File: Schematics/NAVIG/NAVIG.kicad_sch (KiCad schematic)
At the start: 73 parts, among them J1 SWD, J12 GNSS_SMA, J13 3.3V IN, J13 USART, J14 CNTRL I2C, J6 USB_C_Receptacle_USB2.0, SW2 Omron_B3F-10xx, U11 BMP390, U4 BNO055, U4 STM32F205RETx, U7 NEO-M9N, U8 USBLC6-2SC6, Y1 12MHz_ECS-120-18-33-JGN-TR3, Y2 32.768KHz

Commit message: slight fixes to navig board for final production run
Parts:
- added J7: Reset Jumper, Connector_PinHeader_2.54mm:PinHeader_1x02_P2.54mm_Vertical, symbol Connector_Generic:Conn_01x02
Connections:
- net SWD_NRST: now also J7.1 (Pin_1); no longer SW2.1
- new net: J7.2 (Pin_2), SW2.1
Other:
- moved on the sheet: R1, SW2
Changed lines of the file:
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@@
   (junction (at 144.78 38.1) (diameter 0) (color 0 0 0 0)
   )
-  (junction (at 43.18 64.77) (diameter 0) (color 0 0 0 0)
+  (junction (at 43.18 60.96) (diameter 0) (color 0 0 0 0)
   )
   (junction (at 53.34 149.86) (diameter 0) (color 0 0 0 0)
@@
     (stroke (width 0) (type default))
   )
-  (wire (pts (xy 43.18 64.77) (xy 39.37 64.77))
+  (wire (pts (xy 43.18 60.96) (xy 39.37 60.96))
     (stroke (width 0) (type default))
   )
@@
     (stroke (width 0) (type default))
   )
+  (wire (pts (xy 44.45 81.28) (xy 55.88 81.28))
+    (stroke (width 0) (type default))
+  )
   (wire (pts (xy 133.35 38.1) (xy 133.35 36.83))
     (stroke (width 0) (type default))
@@
     (stroke (width 0) (type default))
   )
-  (wire (pts (xy 54.61 64.77) (xy 58.42 64.77))
+  (wire (pts (xy 54.61 60.96) (xy 58.42 60.96))
     (stroke (width 0) (type default))
   )
@@
     (stroke (width 0) (type default))
   )
-  (wire (pts (xy 39.37 81.28) (xy 55.88 81.28))
+  (wire (pts (xy 39.37 81.28) (xy 41.91 81.28))
     (stroke (width 0) (type default))
   )
@@
     (stroke (width 0) (type default))
   )
-  (wire (pts (xy 46.99 64.77) (xy 43.18 64.77))
+  (wire (pts (xy 46.99 60.96) (xy 43.18 60.96))
     (stroke (width 0) (type default))
   )
@@
     (stroke (width 0) (type default))
   )
-  (wire (pts (xy 43.18 58.42) (xy 43.18 64.77))
+  (wire (pts (xy 43.18 54.61) (xy 43.18 60.96))
     (stroke (width 0) (type default))
   )
@@
     (stroke (width 0) (type default))
   )
-  (rectangle (start 25.4 49.53) (end 71.12 73.66)
+  (rectangle (start 25.4 45.72) (end 71.12 69.85)
     (stroke (width 0) (type default))
     (fill (type none))
@@
     (fill (type none))
   )
-  (rectangle (start 25.4 76.2) (end 71.12 95.25)
+  (rectangle (start 25.4 72.39) (end 71.12 95.25)
     (stroke (width 0) (type default))
     (fill (type none))
@@
     (effects (font (size 3 3) bold) (justify left bottom))
   )
-  (text "BOOT0" (at 26.67 53.34 0)
+  (text "BOOT0" (at 26.67 49.53 0)
     (effects (font (size 2 2)) (justify left bottom))
   )
-  (text "MCU RESET" (at 53.34 80.01 0)
+  (text "MCU RESET" (at 53.34 76.2 0)
     (effects (font (size 2 2)) (justify left bottom))
   )
@@
     )
   )
-  (global_label "BOOT0" (shape input) (at 39.37 64.77 180) (fields_autoplaced)
+  (global_label "BOOT0" (shape input) (at 39.37 60.96 180) (fields_autoplaced)
     (effects (font (size 1.27 1.27)) (justify right))
-    (property "Intersheetrefs" "${INTERSHEET_REFS}" (at 30.2767 64.77 0)
+    (property "Intersheetrefs" "${INTERSHEET_REFS}" (at 30.2767 60.96 0)
       (effects (font (size 1.27 1.27)) (justify right) hide)
     )
@@
     )
   )
-  (symbol (lib_id "power:+3.3V") (at 53.34 58.42 270) (unit 1)
+  (symbol (lib_id "power:+3.3V") (at 53.34 54.61 270) (unit 1)
     (in_bom yes) (on_board yes) (dnp no) (fields_autoplaced)
-    (property "Reference" "#PWR07" (at 49.53 58.42 0)
+    (property "Reference" "#PWR07" (at 49.53 54.61 0)
       (effects (font (size 1.27 1.27)) hide)
     )
-    (property "Value" "+3.3V" (at 57.15 58.42 90)
+    (property "Value" "+3.3V" (at 57.15 54.61 90)
       (effects (font (size 1.27 1.27)) (justify left))
     )
-    (property "Footprint" "" (at 53.34 58.42 0)
+    (property "Footprint" "" (at 53.34 54.61 0)
       (effects (font (size 1.27 1.27)) hide)
     )
-    (property "Datasheet" "" (at 53.34 58.42 0)
+    (property "Datasheet" "" (at 53.34 54.61 0)
       (effects (font (size 1.27 1.27)) hide)
     )
@@
     )
   )
-  (symbol (lib_id "power:GND") (at 58.42 64.77 90) (unit 1)
+  (symbol (lib_id "power:GND") (at 58.42 60.96 90) (unit 1)
     (in_bom yes) (on_board yes) (dnp no) (fields_autoplaced)
-    (property "Reference" "#PWR06" (at 64.77 64.77 0)
+    (property "Reference" "#PWR06" (at 64.77 60.96 0)
       (effects (font (size 1.27 1.27)) hide)
     )
-    (property "Value" "GND" (at 62.23 64.77 90)
+    (property "Value" "GND" (at 62.23 60.96 90)
       (effects (font (size 1.27 1.27)) (justify right))
     )
-    (property "Footprint" "" (at 58.42 64.77 0)
+    (property "Footprint" "" (at 58.42 60.96 0)
       (effects (font (size 1.27 1.27)) hide)
     )
-    (property "Datasheet" "" (at 58.42 64.77 0)
+    (property "Datasheet" "" (at 58.42 60.96 0)
       (effects (font (size 1.27 1.27)) hide)
     )
@@
     )
   )
-  (symbol (lib_id "Device:R") (at 50.8 64.77 90) (unit 1)
+  (symbol (lib_id "Device:R") (at 50.8 60.96 90) (unit 1)
     (in_bom yes) (on_board yes) (dnp no)
-    (property "Reference" "R1" (at 50.8 67.31 90)
+    (property "Reference" "R1" (at 50.8 63.5 90)
       (effects (font (size 1.27 1.27)))
     )
-    (property "Value" "100K" (at 50.8 62.23 90)
+    (property "Value" "100K" (at 50.8 58.42 90)
       (effects (font (size 1.27 1.27)))
     )
-    (property "Footprint" "Resistor_SMD:R_0603_1608Metric" (at 50.8 66.548 90)
+    (property "Footprint" "Resistor_SMD:R_0603_1608Metric" (at 50.8 62.738 90)
       (effects (font (size 1.27 1.27)) hide)
     )
-    (property "Datasheet" "~" (at 50.8 64.77 0)
+    (property "Datasheet" "~" (at 50.8 60.96 0)
       (effects (font (size 1.27 1.27)) hide)
     )
@@
     )
   )
+  (symbol (lib_id "Connector_Generic:Conn_01x02") (at 41.91 76.2 90) (unit 1)
+    (in_bom yes) (on_board yes) (dnp no) (fields_autoplaced)
+    (property "Reference" "J7" (at 46.99 74.93 90)
+      (effects (font (size 1.27 1.27)) (justify right))
+    )
+    (property "Value" "Reset Jumper" (at 46.99 77.47 90)
+      (effects (font (size 1.27 1.27)) (justify right))
+    )
+    (property "Footprint" "Connector_PinHeader_2.54mm:PinHeader_1x02_P2.54mm_Vertical" (at 41.91 76.2 0)
+      (effects (font (size 1.27 1.27)) hide)
+    )
+    (property "Datasheet" "~" (at 41.91 76.2 0)
+      (effects (font (size 1.27 1.27)) hide)
+    )
+    (pin "2")
+    (pin "1")
+    (instances
+      (project "NAVIG"
+        (path "/ff004286-2977-49b9-8862-87370f557fdd"
+          (reference "J7") (unit 1)
+        )
+      )
+    )
+  )
   (symbol (lib_id "Mechanical:MountingHole_Pad") (at 359.41 130.81 90) (unit 1)
     (in_bom yes) (on_board yes) (dnp no) (fields_autoplaced)
@@
     )
   )
-  (symbol (lib_id "Switch:SW_Push") (at 48.26 58.42 0) (unit 1)
+  (symbol (lib_id "Switch:SW_Push") (at 48.26 54.61 0) (unit 1)
     (in_bom yes) (on_board yes) (dnp no)
-    (property "Reference" "SW2" (at 43.18 53.34 0)
+    (property "Reference" "SW2" (at 43.18 49.53 0)
       (effects (font (size 1.27 1.27)) (justify left))
     )
-    (property "Value" "Omron_B3F-10xx" (at 49.53 53.34 0)
+    (property "Value" "Omron_B3F-10xx" (at 49.53 49.53 0)
       (effects (font (size 1.27 1.27)) (justify left))
     )
-    (property "Footprint" "Button_Switch_THT:SW_TH_Tactile_Omron_B3F-10xx" (at 48.26 53.34 0)
+    (property "Footprint" "Button_Switch_THT:SW_TH_Tactile_Omron_B3F-10xx" (at 48.26 49.53 0)
       (effects (font (size 1.27 1.27)) hide)
     )
-    (property "Datasheet" "~" (at 48.26 53.34 0)
+    (property "Datasheet" "~" (at 48.26 49.53 0)
       (effects (font (size 1.27 1.27)) hide)
     )

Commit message: final nav
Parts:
- added TP1: 3.3V, TestPoint:TestPoint_Pad_D2.0mm, symbol Connector:TestPoint
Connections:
- net +3.3V: now also TP1.1
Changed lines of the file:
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@@
+    )
+  )
+  (symbol (lib_id "Connector:TestPoint") (at 52.07 193.04 0) (unit 1)
+    (in_bom yes) (on_board yes) (dnp no) (fields_autoplaced)
+    (property "Reference" "TP1" (at 54.61 188.468 0)
+      (effects (font (size 1.27 1.27)) (justify left))
+    )
+    (property "Value" "3.3V" (at 54.61 191.008 0)
+      (effects (font (size 1.27 1.27)) (justify left))
+    )
+    (property "Footprint" "TestPoint:TestPoint_Pad_D2.0mm" (at 57.15 193.04 0)
+      (effects (font (size 1.27 1.27)) hide)
+    )
+    (property "Datasheet" "~" (at 57.15 193.04 0)
+      (effects (font (size 1.27 1.27)) hide)
+    )
+    (pin "1")
+    (instances
+      (project "NAVIG"
+        (path "/ff004286-2977-49b9-8862-87370f557fdd"
+          (reference "TP1") (unit 1)
+        )
+      )
     )
   )
@@
         )
       )
+    )
+  )
+  (symbol (lib_id "power:+3.3V") (at 52.07 193.04 180) (unit 1)
+    (in_bom yes) (on_board yes) (dnp no) (fields_autoplaced)
+    (property "Reference" "#PWR047" (at 52.07 189.23 0)
+      (effects (font (size 1.27 1.27)) hide)
+    )
+    (property "Value" "+3.3V" (at 52.07 198.12 0)
+      (effects (font (size 1.27 1.27)))
+    )
+    (property "Footprint" "" (at 52.07 193.04 0)
+      (effects (font (size 1.27 1.27)) hide)
+    )
+    (property "Datasheet" "" (at 52.07 193.04 0)
+      (effects (font (size 1.27 1.27)) hide)
+    )
+    (pin "1")
+    (instances
+      (project "CNTRL"
+        (path "/1ee9d30d-f96d-431a-b2c2-15cce7e9ab8d"
+          (reference "#PWR047") (unit 1)
+        )
+      )
+      (project "NAVIG"
+        (path "/ff004286-2977-49b9-8862-87370f557fdd"
+          (reference "#PWR025") (unit 1)
+        )
+      )

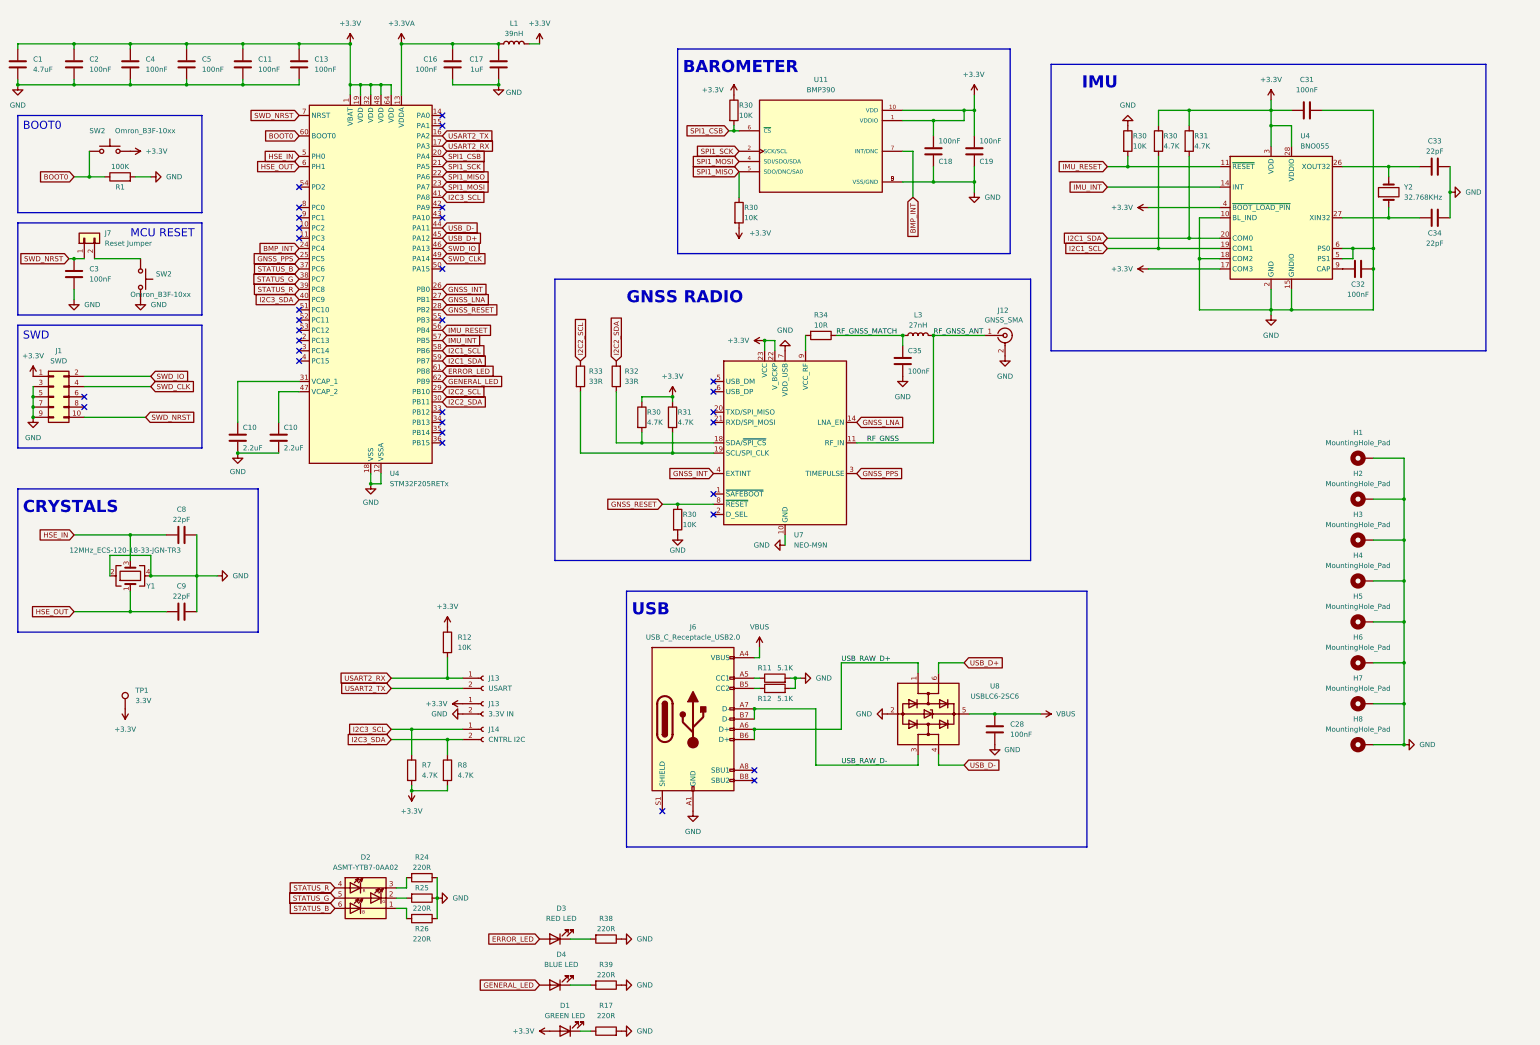
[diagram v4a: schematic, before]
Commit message: initial coding/integration
i2c slave done (kinda doesnt work)
bno055 done (untested)
bmp390 done (untested)
neom9n not done
w25q128jv done (untested)
sd card/fatfs not done
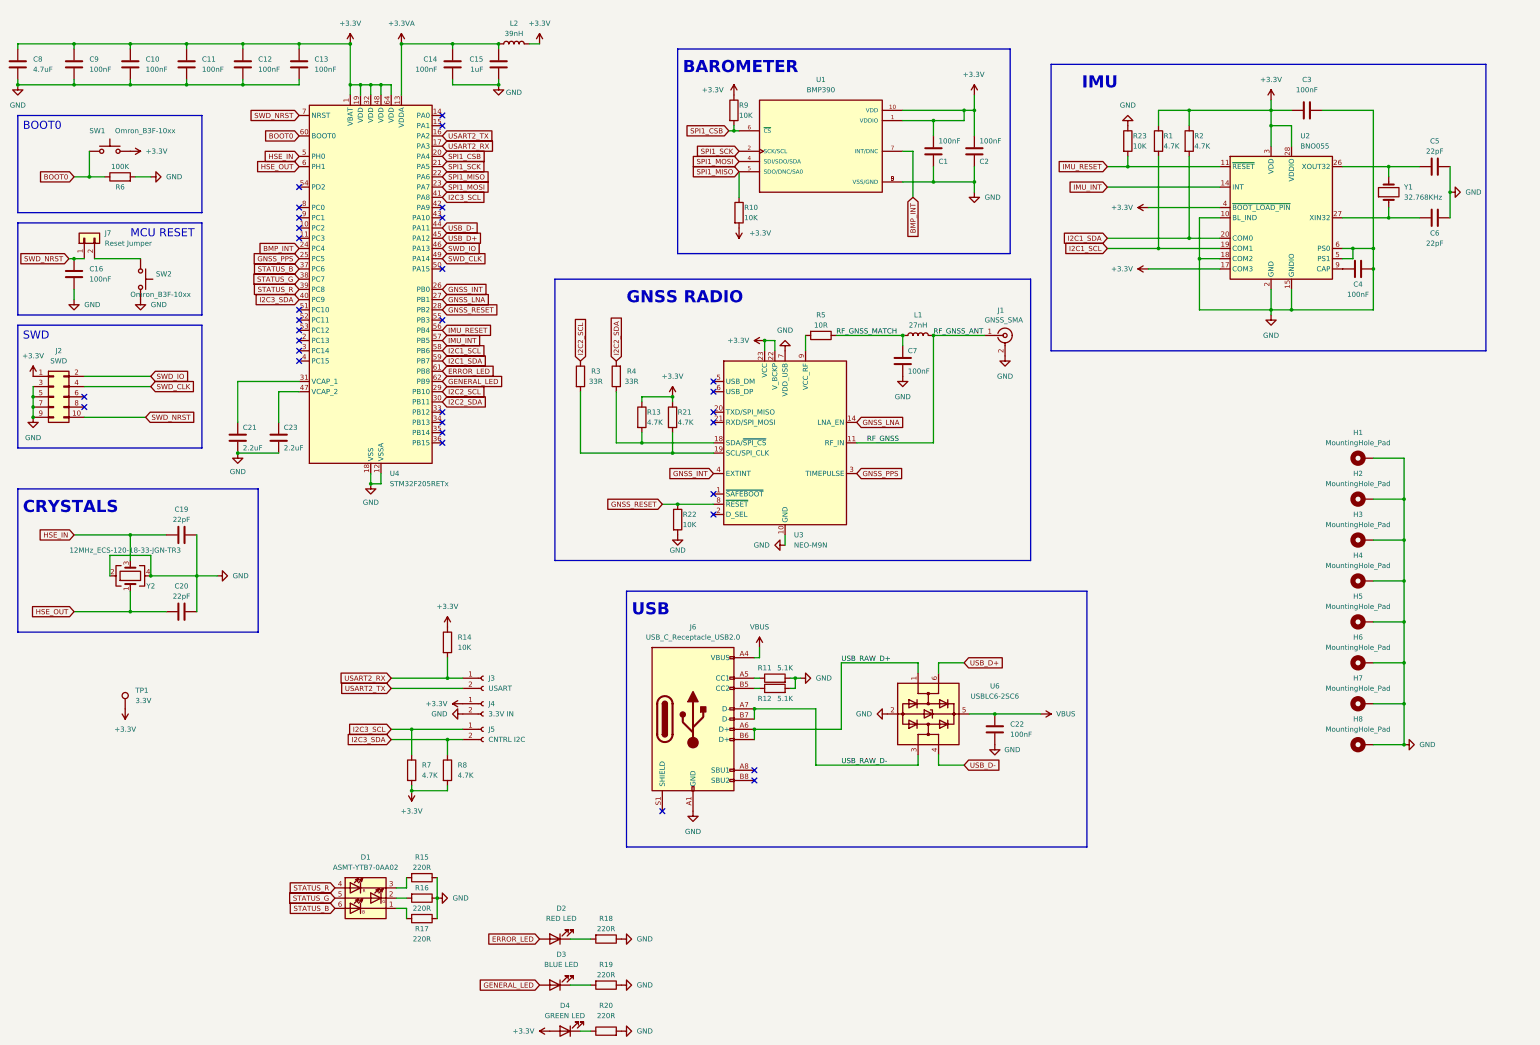
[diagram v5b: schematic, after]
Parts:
- renumbered C18 to C1, C4 to C10, C5 to C11, C11 to C12, C16 to C14, C17 to C15, C3 to C16, C8 to C19, C19 to C2, C9 to C20, C10 to C21, C28 to C22, C10 to C23, C31 to C3, C32 to C4, C33 to C5, C34 to C6, C35 to C7, C1 to C8, C2 to C9, D2 to D1, D3 to D2, D4 to D3, D1 to D4, J12 to J1, J1 to J2, J13 to J3, J13 to J4, J14 to J5, L3 to L1, L1 to L2, R30 to R1, R30 to R10, R30 to R13, R12 to R14, R24 to R15, R25 to R16, R26 to R17, R38 to R18, R39 to R19, R31 to R2, R17 to R20, R31 to R21, R30 to R22, R30 to R23, R33 to R3, R32 to R4, R34 to R5, R1 to R6, R30 to R9, SW2 to SW1, U11 to U1, U4 to U2, U7 to U3, U8 to U6, Y2 to Y1, Y1 to Y2
